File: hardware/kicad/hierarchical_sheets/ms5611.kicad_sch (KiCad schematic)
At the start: 0 parts

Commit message: added ms5611 t o schematic
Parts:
- added U4: MS5611-01BA, Package_LGA:LGA-8_3x5mm_P1.25mm, symbol Sensor_Pressure:MS5611-01BA
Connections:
- new net: U4.4 (CSB), U4.5 (CSB)
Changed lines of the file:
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@@
     (company "Missouri S&T Rocket Design Team")
   )
+  (symbol (lib_id "Sensor_Pressure:MS5611-01BA") (at 99.06 85.09 0) (unit 1)
+    (in_bom yes) (on_board yes) (dnp no) (fields_autoplaced)
+    (property "Reference" "U4" (at 107.95 83.82 0)
+      (effects (font (size 1.27 1.27)) (justify left))
+    )
+    (property "Value" "MS5611-01BA" (at 107.95 86.36 0)
+      (effects (font (size 1.27 1.27)) (justify left))
+    )
+    (property "Footprint" "Package_LGA:LGA-8_3x5mm_P1.25mm" (at 99.06 85.09 0)
+      (effects (font (size 1.27 1.27)) hide)
+    )
+    (property "Datasheet" "https://www.te.com/commerce/DocumentDelivery/DDEController?Action=srchrtrv&DocNm=MS5611-01BA03&DocType=Data+Sheet&DocLang=English" (at 99.06 85.09 0)
+      (effects (font (size 1.27 1.27)) hide)
+    )
+    (pin "1")
+    (pin "2")
+    (pin "3")
+    (pin "4")
+    (pin "5")
+    (pin "6")
+    (pin "7")
+    (pin "8")
+    (instances
+      (project "FC"
+        (path "/54cce219-8b98-4e71-96c4-f9ee784aa3bc/01e59dc5-0a98-4437-b4f9-a1305517a629"
+          (reference "U4") (unit 1)
+        )
+      )
+    )
+  )
 )

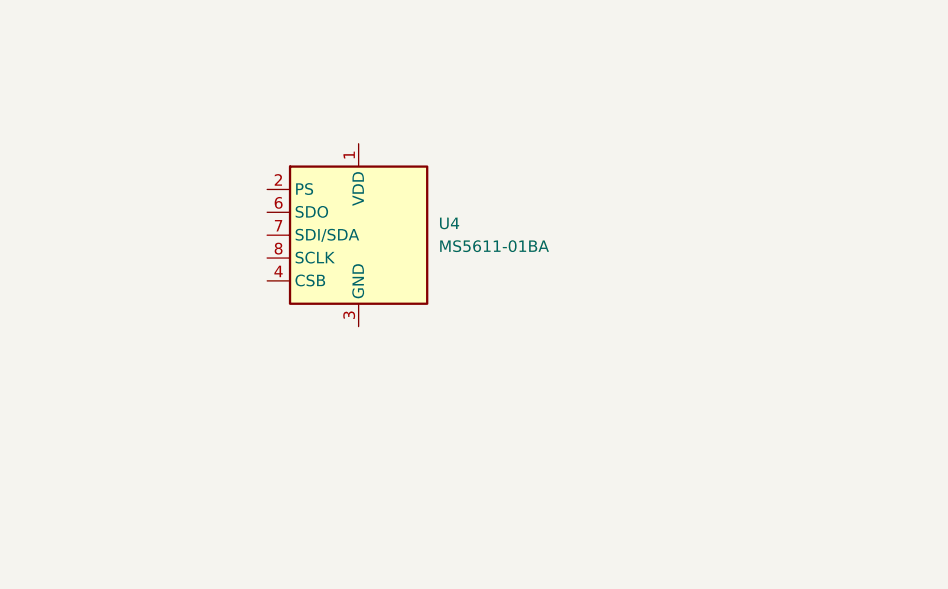
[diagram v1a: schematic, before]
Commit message: updated ms5611 schematic
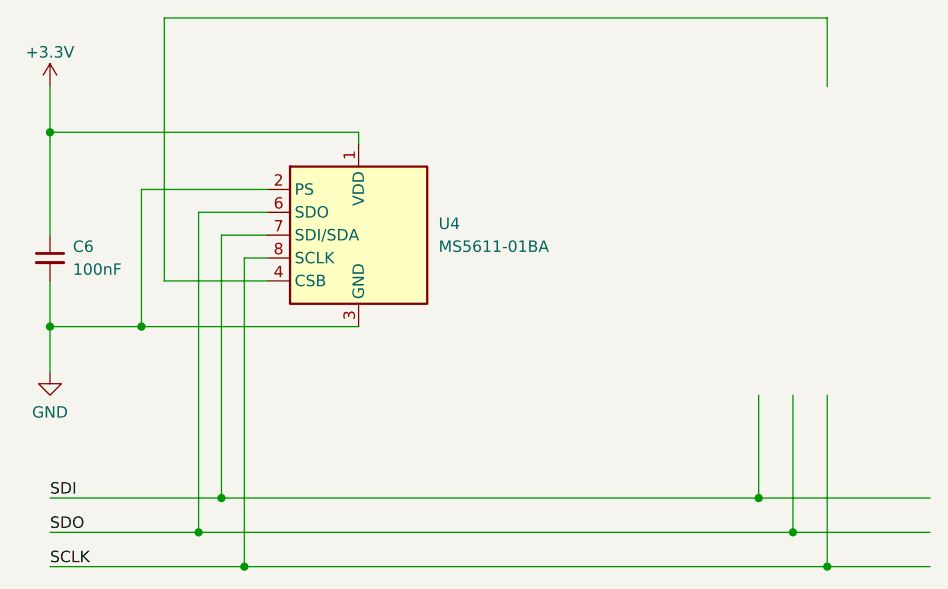
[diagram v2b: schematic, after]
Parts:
- added C6: 100nF, symbol Device:C_Small
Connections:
- net +3.3V: now reaches U4.1 (VDD)
- net +3.3V: now also C6.1
- net GND: now reaches U4.2 (PS)
- net GND: now also U4.3 (GND), C6.2
- net SDO: now reaches U4.6 (SDO)
- net SDI: now reaches U4.7 (SDI/SDA)
- net SCLK: now reaches U4.8 (SCLK)
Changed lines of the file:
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@@
     (company "Missouri S&T Rocket Design Team")
+  )
+  (junction (at 151.13 121.92) (diameter 0) (color 0 0 0 0)
+  )
+  (junction (at 147.32 118.11) (diameter 0) (color 0 0 0 0)
+  )
+  (junction (at 143.51 114.3) (diameter 0) (color 0 0 0 0)
+  )
+  (junction (at 64.77 95.25) (diameter 0) (color 0 0 0 0)
+  )
+  (junction (at 86.36 121.92) (diameter 0) (color 0 0 0 0)
+  )
+  (junction (at 83.82 114.3) (diameter 0) (color 0 0 0 0)
+  )
+  (junction (at 81.28 118.11) (diameter 0) (color 0 0 0 0)
+  )
+  (junction (at 64.77 73.66) (diameter 0) (color 0 0 0 0)
+  )
+  (junction (at 74.93 95.25) (diameter 0) (color 0 0 0 0)
+  )
+  (wire (pts (xy 64.77 114.3) (xy 83.82 114.3))
+    (stroke (width 0) (type default))
+  )
+  (wire (pts (xy 64.77 121.92) (xy 86.36 121.92))
+    (stroke (width 0) (type default))
+  )
+  (wire (pts (xy 88.9 82.55) (xy 81.28 82.55))
+    (stroke (width 0) (type default))
+  )
+  (wire (pts (xy 74.93 95.25) (xy 64.77 95.25))
+    (stroke (width 0) (type default))
+  )
+  (wire (pts (xy 81.28 82.55) (xy 81.28 118.11))
+    (stroke (width 0) (type default))
+  )
+  (wire (pts (xy 77.47 90.17) (xy 77.47 60.96))
+    (stroke (width 0) (type default))
+  )
+  (wire (pts (xy 151.13 102.87) (xy 151.13 121.92))
+    (stroke (width 0) (type default))
+  )
+  (wire (pts (xy 74.93 95.25) (xy 74.93 80.01))
+    (stroke (width 0) (type default))
+  )
+  (wire (pts (xy 99.06 73.66) (xy 99.06 74.93))
+    (stroke (width 0) (type default))
+  )
+  (wire (pts (xy 81.28 118.11) (xy 147.32 118.11))
+    (stroke (width 0) (type default))
+  )
+  (wire (pts (xy 147.32 102.87) (xy 147.32 118.11))
+    (stroke (width 0) (type default))
+  )
+  (wire (pts (xy 151.13 60.96) (xy 151.13 68.58))
+    (stroke (width 0) (type default))
+  )
+  (wire (pts (xy 64.77 90.17) (xy 64.77 95.25))
+    (stroke (width 0) (type default))
+  )
+  (wire (pts (xy 151.13 121.92) (xy 162.56 121.92))
+    (stroke (width 0) (type default))
+  )
+  (wire (pts (xy 64.77 73.66) (xy 64.77 85.09))
+    (stroke (width 0) (type default))
+  )
+  (wire (pts (xy 88.9 90.17) (xy 77.47 90.17))
+    (stroke (width 0) (type default))
+  )
+  (wire (pts (xy 83.82 114.3) (xy 143.51 114.3))
+    (stroke (width 0) (type default))
+  )
+  (wire (pts (xy 143.51 114.3) (xy 162.56 114.3))
+    (stroke (width 0) (type default))
+  )
+  (wire (pts (xy 64.77 118.11) (xy 81.28 118.11))
+    (stroke (width 0) (type default))
+  )
+  (wire (pts (xy 86.36 121.92) (xy 151.13 121.92))
+    (stroke (width 0) (type default))
+  )
+  (wire (pts (xy 143.51 102.87) (xy 143.51 114.3))
+    (stroke (width 0) (type default))
+  )
+  (wire (pts (xy 74.93 80.01) (xy 88.9 80.01))
+    (stroke (width 0) (type default))
+  )
+  (wire (pts (xy 64.77 73.66) (xy 99.06 73.66))
+    (stroke (width 0) (type default))
+  )
+  (wire (pts (xy 88.9 87.63) (xy 86.36 87.63))
+    (stroke (width 0) (type default))
+  )
+  (wire (pts (xy 147.32 118.11) (xy 162.56 118.11))
+    (stroke (width 0) (type default))
+  )
+  (wire (pts (xy 88.9 85.09) (xy 83.82 85.09))
+    (stroke (width 0) (type default))
+  )
+  (wire (pts (xy 83.82 85.09) (xy 83.82 114.3))
+    (stroke (width 0) (type default))
+  )
+  (wire (pts (xy 74.93 95.25) (xy 99.06 95.25))
+    (stroke (width 0) (type default))
+  )
+  (wire (pts (xy 64.77 68.58) (xy 64.77 73.66))
+    (stroke (width 0) (type default))
+  )
+  (wire (pts (xy 64.77 95.25) (xy 64.77 100.33))
+    (stroke (width 0) (type default))
+  )
+  (wire (pts (xy 77.47 60.96) (xy 151.13 60.96))
+    (stroke (width 0) (type default))
+  )
+  (wire (pts (xy 86.36 87.63) (xy 86.36 121.92))
+    (stroke (width 0) (type default))
+  )
+  (label "SCLK" (at 64.77 121.92 0) (fields_autoplaced)
+    (effects (font (size 1.27 1.27)) (justify left bottom))
+  )
+  (label "SDO" (at 64.77 118.11 0) (fields_autoplaced)
+    (effects (font (size 1.27 1.27)) (justify left bottom))
+  )
+  (label "SDI" (at 64.77 114.3 0) (fields_autoplaced)
+    (effects (font (size 1.27 1.27)) (justify left bottom))
+  )
+  (symbol (lib_id "power:GND") (at 64.77 100.33 0) (unit 1)
+    (in_bom yes) (on_board yes) (dnp no) (fields_autoplaced)
+    (property "Reference" "#PWR04" (at 64.77 106.68 0)
+      (effects (font (size 1.27 1.27)) hide)
+    )
+    (property "Value" "GND" (at 64.77 104.775 0)
+      (effects (font (size 1.27 1.27)))
+    )
+    (property "Footprint" "" (at 64.77 100.33 0)
+      (effects (font (size 1.27 1.27)) hide)
+    )
+    (property "Datasheet" "" (at 64.77 100.33 0)
+      (effects (font (size 1.27 1.27)) hide)
+    )
+    (pin "1")
+    (instances
+      (project "FC"
+        (path "/54cce219-8b98-4e71-96c4-f9ee784aa3bc/aac89dea-c005-40db-a234-32c8ed41f1e5"
+          (reference "#PWR04") (unit 1)
+        )
+        (path "/54cce219-8b98-4e71-96c4-f9ee784aa3bc/01e59dc5-0a98-4437-b4f9-a1305517a629"
+          (reference "#PWR07") (unit 1)
+        )
+      )
+    )
+  )
+  (symbol (lib_id "power:+3.3V") (at 64.77 68.58 0) (unit 1)
+    (in_bom yes) (on_board yes) (dnp no)
+    (property "Reference" "#PWR01" (at 64.77 72.39 0)
+      (effects (font (size 1.27 1.27)) hide)
+    )
+    (property "Value" "+3.3V" (at 64.77 64.77 0)
+      (effects (font (size 1.27 1.27)))
+    )
+    (property "Footprint" "" (at 64.77 68.58 0)
+      (effects (font (size 1.27 1.27)) hide)
+    )
+    (property "Datasheet" "" (at 64.77 68.58 0)
+      (effects (font (size 1.27 1.27)) hide)
+    )
+    (pin "1")
+    (instances
+      (project "FC"
+        (path "/54cce219-8b98-4e71-96c4-f9ee784aa3bc/aac89dea-c005-40db-a234-32c8ed41f1e5"
+          (reference "#PWR01") (unit 1)
+        )
+        (path "/54cce219-8b98-4e71-96c4-f9ee784aa3bc/01e59dc5-0a98-4437-b4f9-a1305517a629"
+          (reference "#PWR05") (unit 1)
+        )
+      )
+    )
   )
   (symbol (lib_id "Sensor_Pressure:MS5611-01BA") (at 99.06 85.09 0) (unit 1)
@@
         )
       )
+    )
+  )
+  (symbol (lib_id "Device:C_Small") (at 64.77 87.63 0) (unit 1)
+    (in_bom yes) (on_board yes) (dnp no) (fields_autoplaced)
+    (property "Reference" "C6" (at 67.31 86.3663 0)
+      (effects (font (size 1.27 1.27)) (justify left))
+    )
+    (property "Value" "100nF" (at 67.31 88.9063 0)
+      (effects (font (size 1.27 1.27)) (justify left))
+    )
+    (property "Footprint" "" (at 64.77 87.63 0)
+      (effects (font (size 1.27 1.27)) hide)
+    )
+    (property "Datasheet" "~" (at 64.77 87.63 0)
+      (effects (font (size 1.27 1.27)) hide)
+    )
+    (pin "1")
+    (pin "2")
+    (instances
+      (project "FC"
+        (path "/54cce219-8b98-4e71-96c4-f9ee784aa3bc/01e59dc5-0a98-4437-b4f9-a1305517a629"
+          (reference "C6") (unit 1)
+        )
+      )

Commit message: Storage Updated
Didn't save. Added pins to hierarchal sheets. In/Out
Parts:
- removed C6: 100nF, symbol Device:C_Small
- removed U4: MS5611-01BA, Package_LGA:LGA-8_3x5mm_P1.25mm, symbol Sensor_Pressure:MS5611-01BA
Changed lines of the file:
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@@
     (company "Missouri S&T Rocket Design Team")
   )
-  (junction (at 151.13 121.92) (diameter 0) (color 0 0 0 0)
-  )
-  (junction (at 147.32 118.11) (diameter 0) (color 0 0 0 0)
-  )
-  (junction (at 143.51 114.3) (diameter 0) (color 0 0 0 0)
-  )
-  (junction (at 64.77 95.25) (diameter 0) (color 0 0 0 0)
-  )
-  (junction (at 86.36 121.92) (diameter 0) (color 0 0 0 0)
-  )
-  (junction (at 83.82 114.3) (diameter 0) (color 0 0 0 0)
-  )
-  (junction (at 81.28 118.11) (diameter 0) (color 0 0 0 0)
-  )
-  (junction (at 64.77 73.66) (diameter 0) (color 0 0 0 0)
-  )
-  (junction (at 74.93 95.25) (diameter 0) (color 0 0 0 0)
-  )
-  (wire (pts (xy 64.77 114.3) (xy 83.82 114.3))
-    (stroke (width 0) (type default))
-  )
-  (wire (pts (xy 64.77 121.92) (xy 86.36 121.92))
-    (stroke (width 0) (type default))
-  )
-  (wire (pts (xy 88.9 82.55) (xy 81.28 82.55))
-    (stroke (width 0) (type default))
-  )
-  (wire (pts (xy 74.93 95.25) (xy 64.77 95.25))
-    (stroke (width 0) (type default))
-  )
-  (wire (pts (xy 81.28 82.55) (xy 81.28 118.11))
-    (stroke (width 0) (type default))
-  )
-  (wire (pts (xy 77.47 90.17) (xy 77.47 60.96))
-    (stroke (width 0) (type default))
-  )
-  (wire (pts (xy 151.13 102.87) (xy 151.13 121.92))
-    (stroke (width 0) (type default))
-  )
-  (wire (pts (xy 74.93 95.25) (xy 74.93 80.01))
-    (stroke (width 0) (type default))
-  )
-  (wire (pts (xy 99.06 73.66) (xy 99.06 74.93))
-    (stroke (width 0) (type default))
-  )
-  (wire (pts (xy 81.28 118.11) (xy 147.32 118.11))
-    (stroke (width 0) (type default))
-  )
-  (wire (pts (xy 147.32 102.87) (xy 147.32 118.11))
-    (stroke (width 0) (type default))
-  )
-  (wire (pts (xy 151.13 60.96) (xy 151.13 68.58))
-    (stroke (width 0) (type default))
-  )
-  (wire (pts (xy 64.77 90.17) (xy 64.77 95.25))
-    (stroke (width 0) (type default))
-  )
-  (wire (pts (xy 151.13 121.92) (xy 162.56 121.92))
-    (stroke (width 0) (type default))
-  )
-  (wire (pts (xy 64.77 73.66) (xy 64.77 85.09))
-    (stroke (width 0) (type default))
-  )
-  (wire (pts (xy 88.9 90.17) (xy 77.47 90.17))
-    (stroke (width 0) (type default))
-  )
-  (wire (pts (xy 83.82 114.3) (xy 143.51 114.3))
-    (stroke (width 0) (type default))
-  )
-  (wire (pts (xy 143.51 114.3) (xy 162.56 114.3))
-    (stroke (width 0) (type default))
-  )
-  (wire (pts (xy 64.77 118.11) (xy 81.28 118.11))
-    (stroke (width 0) (type default))
-  )
-  (wire (pts (xy 86.36 121.92) (xy 151.13 121.92))
-    (stroke (width 0) (type default))
-  )
-  (wire (pts (xy 143.51 102.87) (xy 143.51 114.3))
-    (stroke (width 0) (type default))
-  )
-  (wire (pts (xy 74.93 80.01) (xy 88.9 80.01))
-    (stroke (width 0) (type default))
-  )
-  (wire (pts (xy 64.77 73.66) (xy 99.06 73.66))
-    (stroke (width 0) (type default))
-  )
-  (wire (pts (xy 88.9 87.63) (xy 86.36 87.63))
-    (stroke (width 0) (type default))
-  )
-  (wire (pts (xy 147.32 118.11) (xy 162.56 118.11))
-    (stroke (width 0) (type default))
-  )
-  (wire (pts (xy 88.9 85.09) (xy 83.82 85.09))
-    (stroke (width 0) (type default))
-  )
-  (wire (pts (xy 83.82 85.09) (xy 83.82 114.3))
-    (stroke (width 0) (type default))
-  )
-  (wire (pts (xy 74.93 95.25) (xy 99.06 95.25))
-    (stroke (width 0) (type default))
-  )
-  (wire (pts (xy 64.77 68.58) (xy 64.77 73.66))
-    (stroke (width 0) (type default))
-  )
-  (wire (pts (xy 64.77 95.25) (xy 64.77 100.33))
-    (stroke (width 0) (type default))
-  )
-  (wire (pts (xy 77.47 60.96) (xy 151.13 60.96))
-    (stroke (width 0) (type default))
-  )
-  (wire (pts (xy 86.36 87.63) (xy 86.36 121.92))
-    (stroke (width 0) (type default))
-  )
-  (label "SCLK" (at 64.77 121.92 0) (fields_autoplaced)
-    (effects (font (size 1.27 1.27)) (justify left bottom))
-  )
-  (label "SDO" (at 64.77 118.11 0) (fields_autoplaced)
-    (effects (font (size 1.27 1.27)) (justify left bottom))
-  )
-  (label "SDI" (at 64.77 114.3 0) (fields_autoplaced)
-    (effects (font (size 1.27 1.27)) (justify left bottom))
-  )
-  (symbol (lib_id "power:GND") (at 64.77 100.33 0) (unit 1)
-    (in_bom yes) (on_board yes) (dnp no) (fields_autoplaced)
-    (property "Reference" "#PWR04" (at 64.77 106.68 0)
-      (effects (font (size 1.27 1.27)) hide)
-    )
-    (property "Value" "GND" (at 64.77 104.775 0)
-      (effects (font (size 1.27 1.27)))
-    )
-    (property "Footprint" "" (at 64.77 100.33 0)
-      (effects (font (size 1.27 1.27)) hide)
-    )
-    (property "Datasheet" "" (at 64.77 100.33 0)
-      (effects (font (size 1.27 1.27)) hide)
-    )
-    (pin "1")
-    (instances
-      (project "FC"
-        (path "/54cce219-8b98-4e71-96c4-f9ee784aa3bc/aac89dea-c005-40db-a234-32c8ed41f1e5"
-          (reference "#PWR04") (unit 1)
-        )
-        (path "/54cce219-8b98-4e71-96c4-f9ee784aa3bc/01e59dc5-0a98-4437-b4f9-a1305517a629"
-          (reference "#PWR07") (unit 1)
-        )
-      )
-    )
-  )
-  (symbol (lib_id "power:+3.3V") (at 64.77 68.58 0) (unit 1)
-    (in_bom yes) (on_board yes) (dnp no)
-    (property "Reference" "#PWR01" (at 64.77 72.39 0)
-      (effects (font (size 1.27 1.27)) hide)
-    )
-    (property "Value" "+3.3V" (at 64.77 64.77 0)
-      (effects (font (size 1.27 1.27)))
-    )
-    (property "Footprint" "" (at 64.77 68.58 0)
-      (effects (font (size 1.27 1.27)) hide)
-    )
-    (property "Datasheet" "" (at 64.77 68.58 0)
-      (effects (font (size 1.27 1.27)) hide)
-    )
-    (pin "1")
-    (instances
-      (project "FC"
-        (path "/54cce219-8b98-4e71-96c4-f9ee784aa3bc/aac89dea-c005-40db-a234-32c8ed41f1e5"
-          (reference "#PWR01") (unit 1)
-        )
-        (path "/54cce219-8b98-4e71-96c4-f9ee784aa3bc/01e59dc5-0a98-4437-b4f9-a1305517a629"
-          (reference "#PWR05") (unit 1)
-        )
-      )
-    )
-  )
-  (symbol (lib_id "Sensor_Pressure:MS5611-01BA") (at 99.06 85.09 0) (unit 1)
-    (in_bom yes) (on_board yes) (dnp no) (fields_autoplaced)
-    (property "Reference" "U4" (at 107.95 83.82 0)
-      (effects (font (size 1.27 1.27)) (justify left))
-    )
-    (property "Value" "MS5611-01BA" (at 107.95 86.36 0)
-      (effects (font (size 1.27 1.27)) (justify left))
-    )
-    (property "Footprint" "Package_LGA:LGA-8_3x5mm_P1.25mm" (at 99.06 85.09 0)
-      (effects (font (size 1.27 1.27)) hide)
-    )
-    (property "Datasheet" "https://www.te.com/commerce/DocumentDelivery/DDEController?Action=srchrtrv&DocNm=MS5611-01BA03&DocType=Data+Sheet&DocLang=English" (at 99.06 85.09 0)
-      (effects (font (size 1.27 1.27)) hide)
-    )
-    (pin "1")
-    (pin "2")
-    (pin "3")
-    (pin "4")
-    (pin "5")
-    (pin "6")
-    (pin "7")
-    (pin "8")
-    (instances
-      (project "FC"
-        (path "/54cce219-8b98-4e71-96c4-f9ee784aa3bc/01e59dc5-0a98-4437-b4f9-a1305517a629"
-          (reference "U4") (unit 1)
-        )
-      )
-    )
-  )
-  (symbol (lib_id "Device:C_Small") (at 64.77 87.63 0) (unit 1)
-    (in_bom yes) (on_board yes) (dnp no) (fields_autoplaced)
-    (property "Reference" "C6" (at 67.31 86.3663 0)
-      (effects (font (size 1.27 1.27)) (justify left))
-    )
-    (property "Value" "100nF" (at 67.31 88.9063 0)
-      (effects (font (size 1.27 1.27)) (justify left))
-    )
-    (property "Footprint" "" (at 64.77 87.63 0)
-      (effects (font (size 1.27 1.27)) hide)
-    )
-    (property "Datasheet" "~" (at 64.77 87.63 0)
-      (effects (font (size 1.27 1.27)) hide)
-    )
-    (pin "1")
-    (pin "2")
-    (instances
-      (project "FC"
-        (path "/54cce219-8b98-4e71-96c4-f9ee784aa3bc/01e59dc5-0a98-4437-b4f9-a1305517a629"
-          (reference "C6") (unit 1)
-        )
-      )
-    )
-  )
 )
